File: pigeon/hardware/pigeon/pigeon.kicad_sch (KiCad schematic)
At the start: 0 parts

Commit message: started pigeon schematic
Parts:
- added C1: 100nF, symbol Device:C
- added J1: Battery, Connector_JST:JST_PH_S2B-PH-K_1x02_P2.00mm_Horizontal, symbol Connector:Conn_01x02_Pin
- added R1, R2: 100k, symbol Device:R
- added SW1: Power Switch, symbol Switch:SW_SPDT
- added TP1: VBAT, symbol Connector:TestPoint
- added TP2: GND, symbol Connector:TestPoint
- added U1: ESP32-S3-Zero, AVES:Waveshare-ESP32-S3-Zero, symbol AVES:ESP32-S3-Zero
- added U2: Adafruit_Ultimate_GPS, AVES:Adafruit_Ultimate_GPS, symbol AVES:Adafruit_Ultimate_GPS
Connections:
- new net: J1.1 (Pin_1), SW1.2 (B)
- new net: C1.2, R2.1
- new net +3V3: U1.3 (3V3(OUT)), U2.8 (VIN)
- new net GND: J1.2 (Pin_2), R2.2, TP2.1, U1.2 (GND), U2.7 (GND)
- new net GPS_RX: U1.15 (GPIO12), U2.6 (RX)
- new net GPS_TX: U1.16 (GPIO13), U2.5 (TX)
- new net VBAT: R1.1, SW1.3 (C), TP1.1, U1.1 (VIN)
- new net VBAT_SENSE: C1.1, R1.2

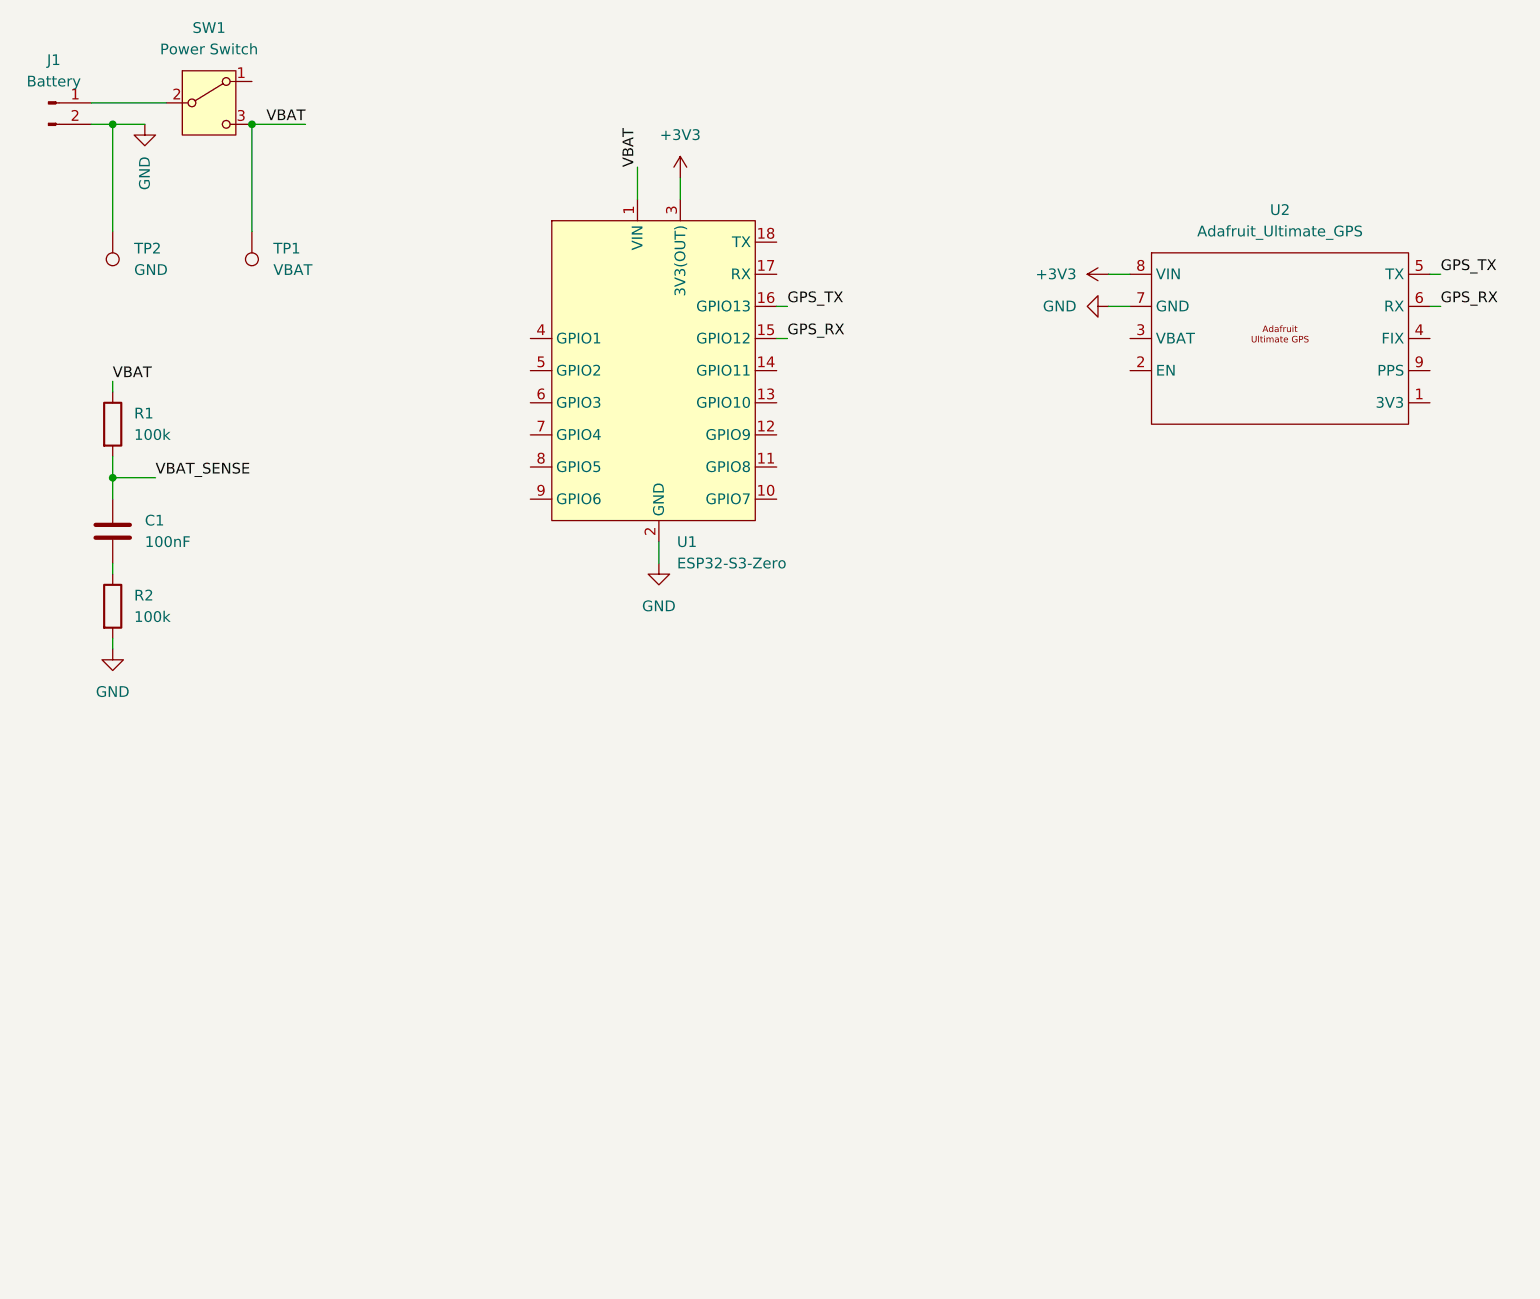
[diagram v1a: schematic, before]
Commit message: added custom adafruit rfm95w symbols and footprints
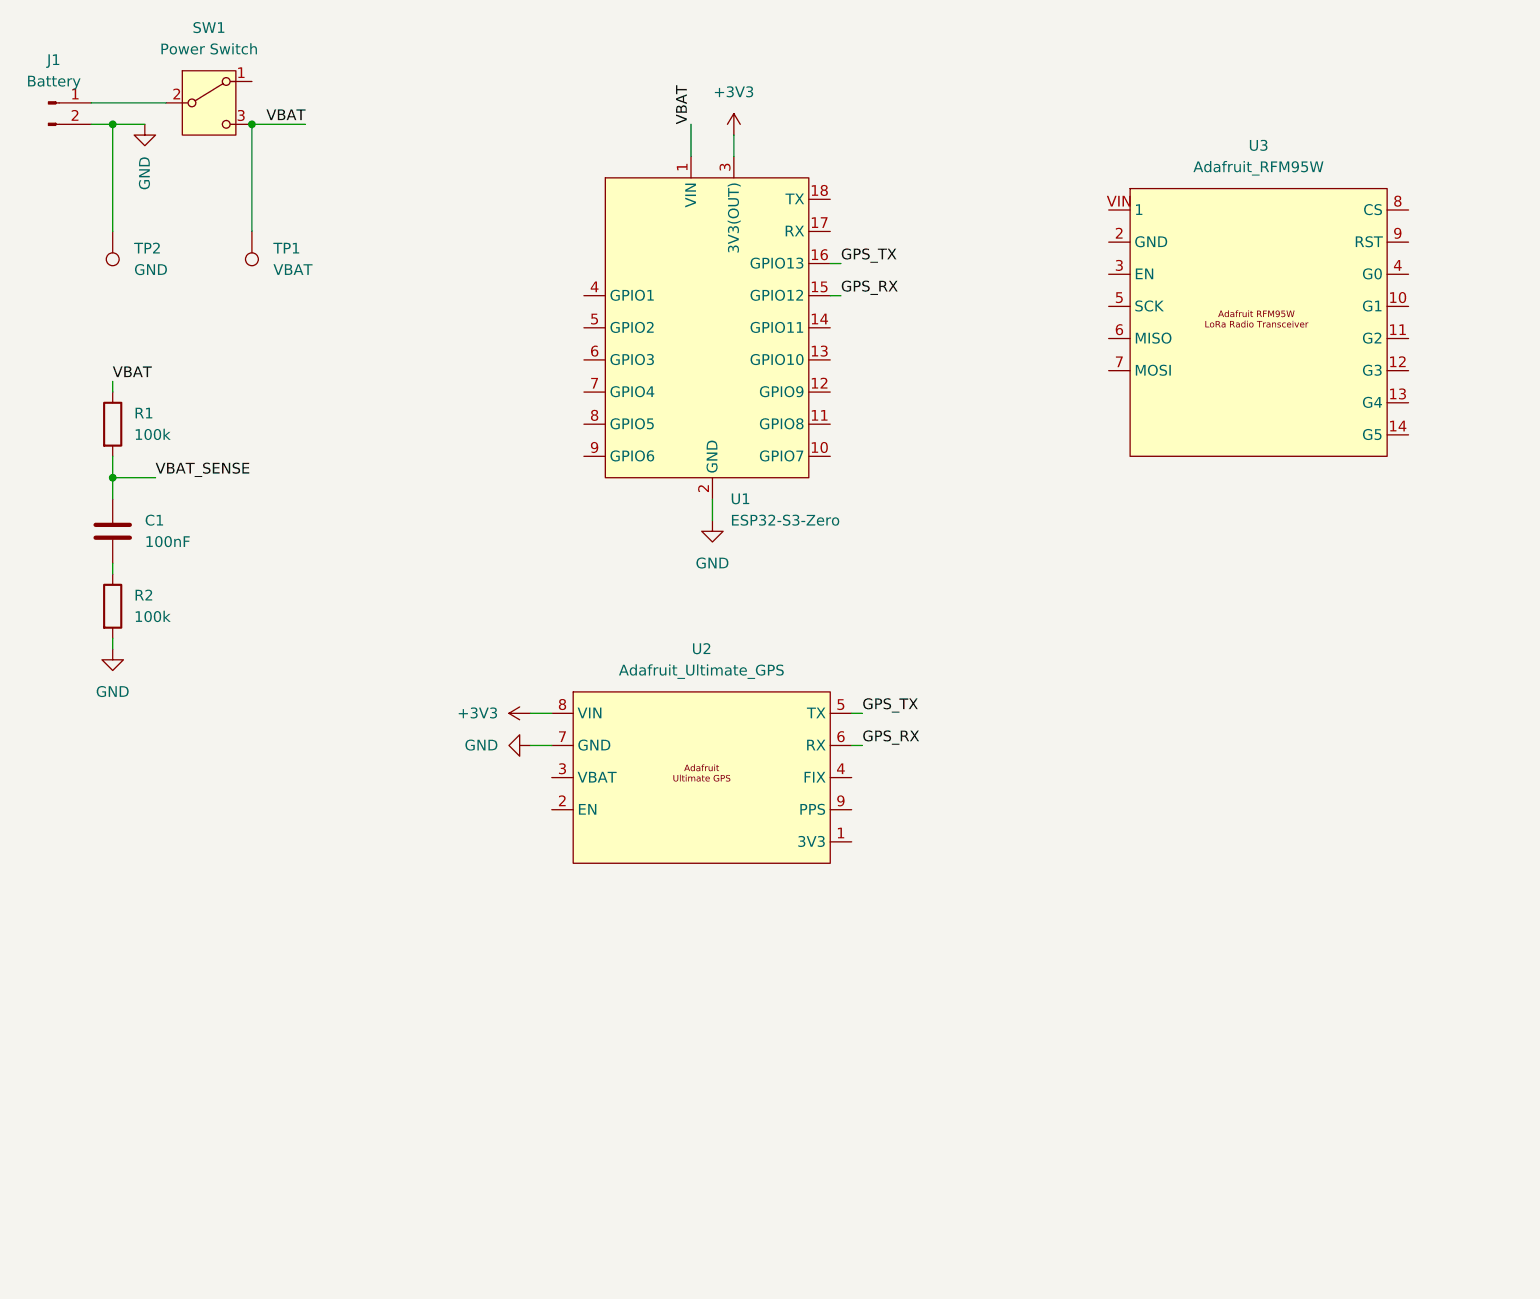
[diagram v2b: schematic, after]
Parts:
- added U3: Adafruit_RFM95W, symbol AVES:Adafruit_RFM95W
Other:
- moved on the sheet: U1

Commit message: pigeon: updated pin assignments
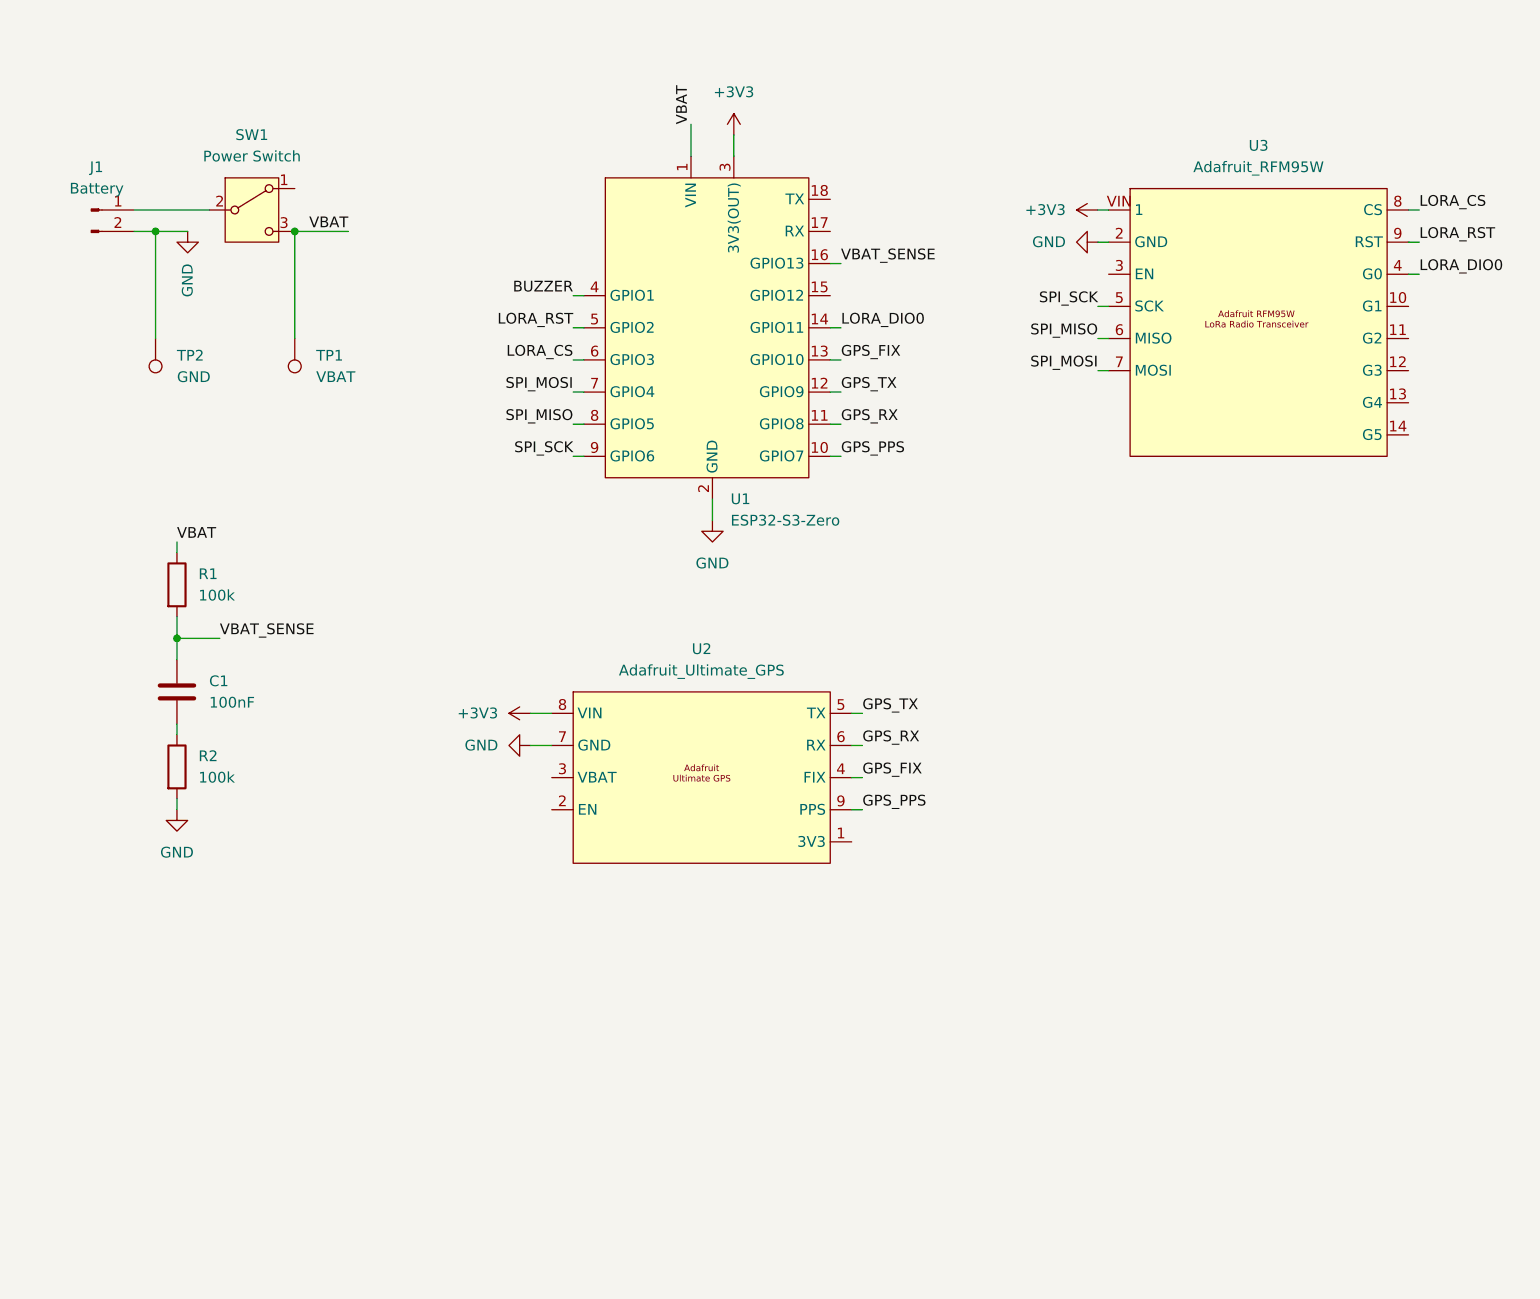
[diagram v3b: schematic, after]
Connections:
- net +3V3: now also U3.VIN (1)
- net GND: now also U3.2 (GND)
- net GPS_RX: now also U1.11 (GPIO8); no longer U1.15 (GPIO12)
- net GPS_TX: now also U1.12 (GPIO9); no longer U1.16 (GPIO13)
- net VBAT_SENSE: now also U1.16 (GPIO13)
- net GPS_FIX: now reaches U2.4 (FIX)
- net GPS_FIX: now also U1.13 (GPIO10)
- net GPS_PPS: now reaches U2.9 (PPS)
- net GPS_PPS: now also U1.10 (GPIO7)
- net LORA_DIO0: now reaches U3.4 (G0)
- net LORA_DIO0: now also U1.14 (GPIO11)
- net SPI_SCK: now reaches U3.5 (SCK)
- net SPI_SCK: now also U1.9 (GPIO6)
- net SPI_MISO: now reaches U3.6 (MISO)
- net SPI_MISO: now also U1.8 (GPIO5)
- net SPI_MOSI: now reaches U3.7 (MOSI)
- net SPI_MOSI: now also U1.7 (GPIO4)
- net LORA_CS: now reaches U3.8 (CS)
- net LORA_CS: now also U1.6 (GPIO3)
- net LORA_RST: now reaches U3.9 (RST)
- net LORA_RST: now also U1.5 (GPIO2)
- net BUZZER: now reaches U1.4 (GPIO1)
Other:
- moved on the sheet: C1, J1, R1, R2, SW1, TP1, TP2

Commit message: pigeon: started pcb
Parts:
- added BZ1: AST1341MCTRQ, AVES:BZ_AST1341MCTRQ, symbol Device:Buzzer
- added C2: 10uF, Capacitor_SMD:C_0805_2012Metric_Pad1.18x1.45mm_HandSolder, symbol Device:C
- C1: footprint (none) -> Capacitor_SMD:C_0805_2012Metric_Pad1.18x1.45mm_HandSolder
- R1, R2: footprint (none) -> Resistor_SMD:R_0805_2012Metric_Pad1.20x1.40mm_HandSolder
- SW1: footprint (none) -> AVES:SW_CK_JS102011SAQN
- TP1, TP2: footprint (none) -> TestPoint:TestPoint_Pad_D2.0mm
- U3: footprint (none) -> AVES:Adafruit_RFM95W
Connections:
- net +3V3: now also U3.1 (VIN); no longer U3.VIN (1)
- net BUZZER: now also U1.9 (GPIO6), BZ1.1 (+); no longer U1.4 (GPIO1)
- net GND: now also BZ1.2 (-), C2.1
- net GPS_FIX: now also U1.8 (GPIO5); no longer U1.13 (GPIO10)
- net GPS_PPS: now also U1.5 (GPIO2); no longer U1.10 (GPIO7)
- net GPS_RX: now also U1.6 (GPIO3); no longer U1.11 (GPIO8)
- net GPS_TX: now also U1.7 (GPIO4); no longer U1.12 (GPIO9)
- net LORA_CS: now also U1.11 (GPIO8); no longer U1.6 (GPIO3)
- net LORA_DIO0: now also U1.15 (GPIO12); no longer U1.14 (GPIO11)
- net LORA_RST: now also U1.10 (GPIO7); no longer U1.5 (GPIO2)
- net SPI_MISO: now also U1.13 (GPIO10); no longer U1.8 (GPIO5)
- net SPI_MOSI: now also U1.12 (GPIO9); no longer U1.7 (GPIO4)
- net SPI_SCK: now also U1.14 (GPIO11); no longer U1.9 (GPIO6)
- net VBAT: now also C2.2
- net VBAT_SENSE: now also U1.4 (GPIO1); no longer U1.16 (GPIO13)
- no-connect marks 0 -> 13
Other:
- moved on the sheet: U1, U2, U3

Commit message: pigeon: pcb layout mostly completed. Layed everything out and added mounting holes
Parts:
- added MH1, MH2, MH3, MH4: MountingHole_Pad, MountingHole:MountingHole_2.2mm_M2_Pad_Via, symbol Mechanical:MountingHole_Pad
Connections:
- net GND: now also MH1.1, MH2.1, MH3.1, MH4.1

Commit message: pigeon: version 1 of pcb
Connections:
- net GPS_FIX: now also U1.7 (GPIO4); no longer U1.8 (GPIO5)
- net GPS_PPS: now also U1.8 (GPIO5); no longer U1.5 (GPIO2)
- net GPS_RX: now also U1.5 (GPIO2); no longer U1.6 (GPIO3)
- net GPS_TX: now also U1.6 (GPIO3); no longer U1.7 (GPIO4)
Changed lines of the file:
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@@
 	)
 	(label "GPS_FIX"
-		(at 81.28 62.23 180)
+		(at 81.28 58.42 180)
 		(effects
 			(font
@@
 	)
 	(label "GPS_RX"
-		(at 81.28 54.61 180)
+		(at 81.28 50.8 180)
 		(effects
 			(font
@@
 	)
 	(label "GPS_PPS"
-		(at 81.28 50.8 180)
+		(at 81.28 62.23 180)
 		(effects
 			(font
@@
 	)
 	(label "GPS_TX"
-		(at 81.28 58.42 180)
+		(at 81.28 54.61 180)
 		(effects
 			(font

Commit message: pigeon: updated pcb to include mode switch
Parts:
- added SW2: Mode Switch, AVES:SW_CK_JS102011SAQN, symbol Switch:SW_SPDT
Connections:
- net +3V3: now also SW2.1 (A)
- net GND: now also SW2.3 (C)
- net MODE_SW: now reaches U1.16 (GPIO13)
- net MODE_SW: now also SW2.2 (B)
- no-connect marks 13 -> 12
